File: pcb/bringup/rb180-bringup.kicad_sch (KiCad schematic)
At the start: 55 parts, among them J1 GT-USB-7010B, J2 Conn_02x03, J3 Conn_02x01, SW1 SKRPACE010, SW2 SKRPACE010, U2 NCP115ASN330, U4 W25Q128JVSS, U6 SN74LVC8T245, U7 SN74LVC8T245, U8 SN74LVC8T245, Y1 12 MHz

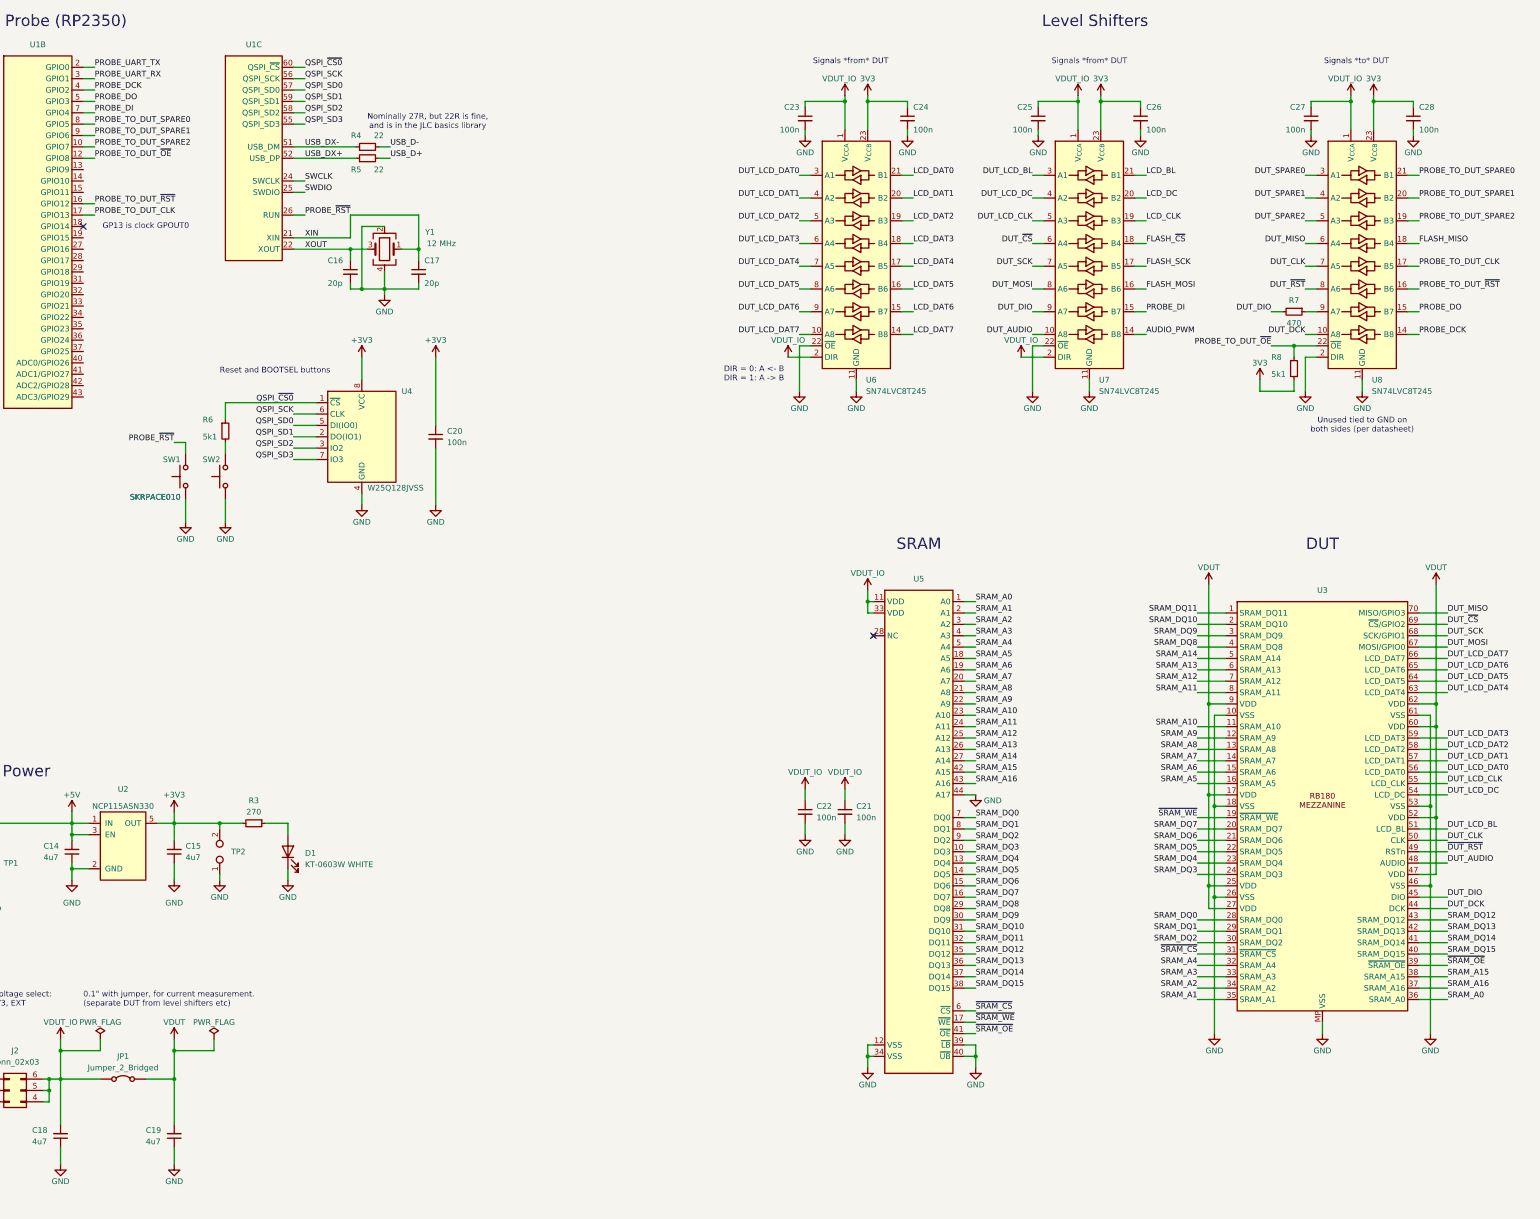
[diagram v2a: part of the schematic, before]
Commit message: Add LCD header and control muxing jumpers
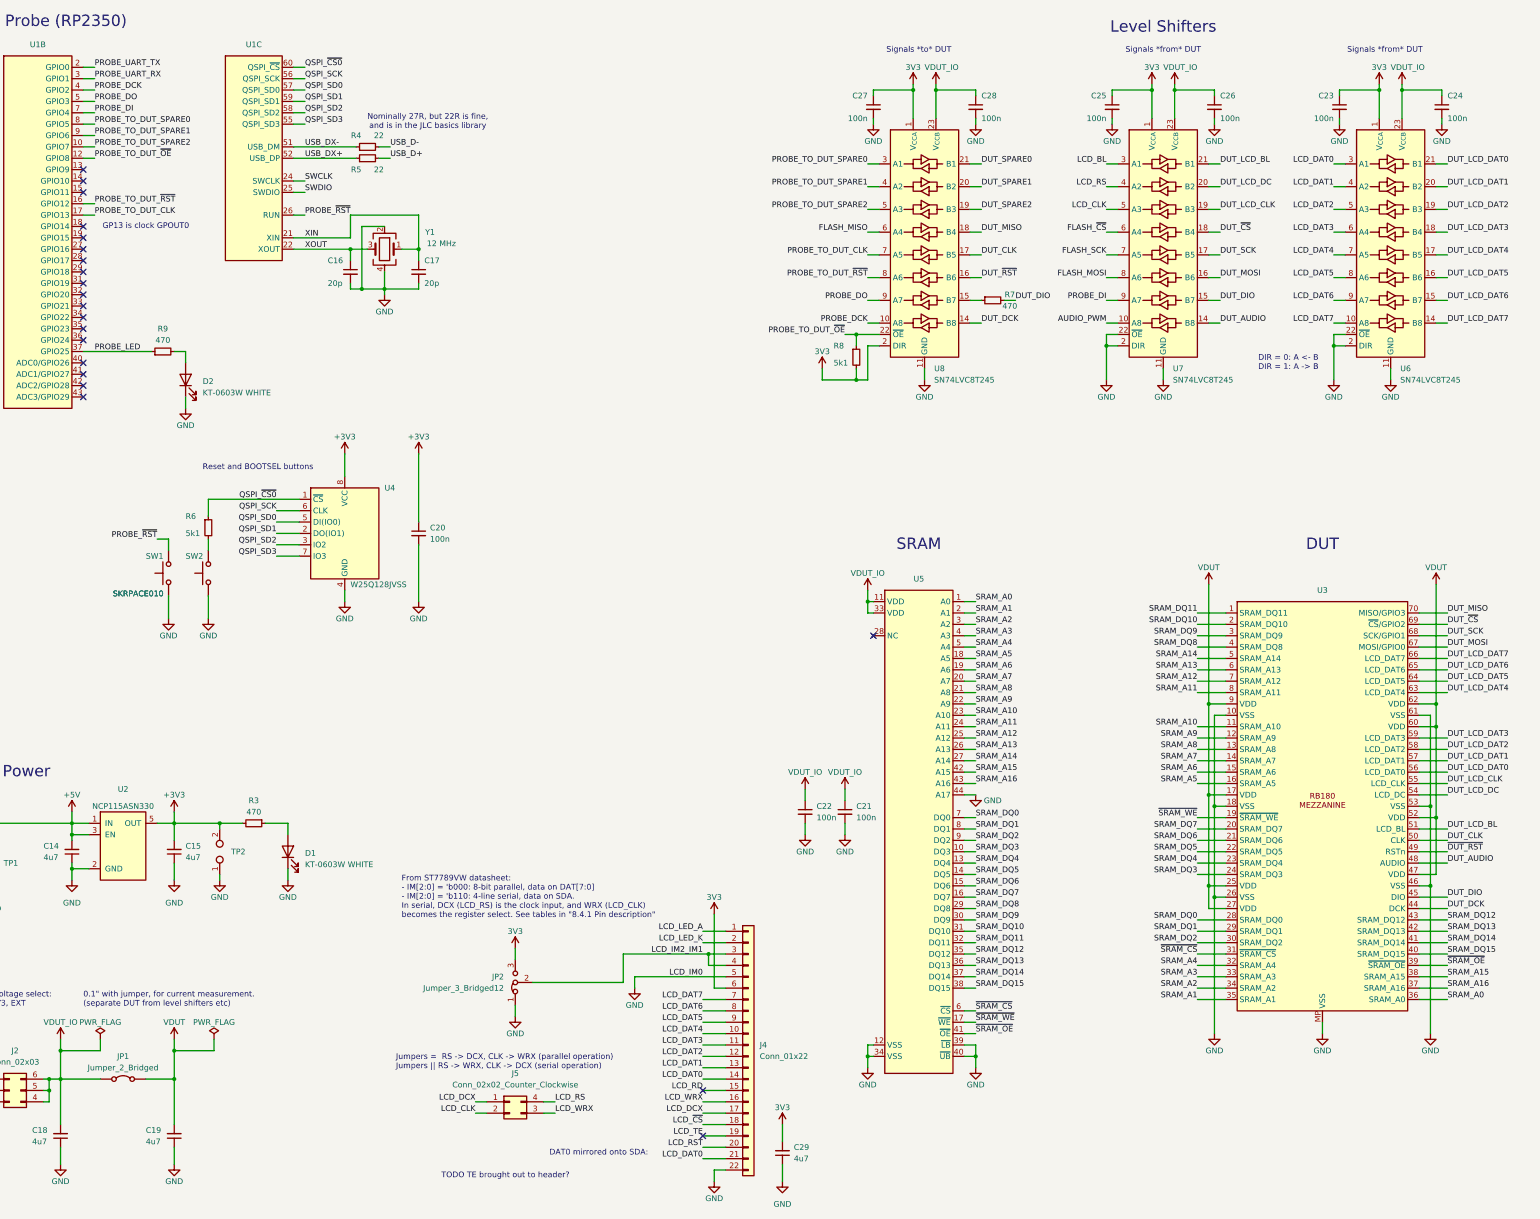
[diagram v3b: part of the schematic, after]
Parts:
- added C29: 4u7, Capacitor_SMD:C_0402_1005Metric, symbol Device:C_Small
- added D2: KT-0603W WHITE, LED_SMD:LED_0603_1608Metric, symbol Device:LED
- added J4: Conn_01x22, symbol Connector_Generic:Conn_01x22
- added J5: Conn_02x02_Counter_Clockwise, symbol Connector_Generic:Conn_02x02_Counter_Clockwise
- added JP2: Jumper_3_Bridged12, symbol Jumper:Jumper_3_Bridged12
- added R9: 470, Resistor_SMD:R_0402_1005Metric, symbol Device:R_Small
- R3: value 270 -> 470; LCSC C352448 -> (none)
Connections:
- net LCD_DC is gone; now on net DUT_LCD_DC: U7.20 (B2)
- net 3V3: now also C23.1, C25.1, C27.1, U6.1 (V_{CCA}), U7.1 (V_{CCA}), U8.1 (V_{CCA}), U8.2 (DIR), C29.2, J4.6 (Pin_6), JP2.3 (B); no longer C24.1, C26.1, C28.1, U6.23 (V_{CCB}), U6.24 (V_{CCB}), U7.23 (V_{CCB}), U7.24 (V_{CCB}), U8.23 (V_{CCB}), U8.24 (V_{CCB})
- net AUDIO_PWM: now also U7.10 (A8); no longer U7.14 (B8)
- net DUT_AUDIO: now also U7.14 (B8); no longer U7.10 (A8)
- net DUT_CLK: now also U8.17 (B5); no longer U8.7 (A5)
- net DUT_DCK: now also U8.14 (B8); no longer U8.10 (A8)
- net DUT_DIO: now also U7.15 (B7); no longer U7.9 (A7)
- net DUT_LCD_BL: now also U7.21 (B1); no longer U7.3 (A1)
- net DUT_LCD_CLK: now also U7.19 (B3); no longer U7.5 (A3)
- net DUT_LCD_DAT0: now also U6.21 (B1); no longer U6.3 (A1)
- net DUT_LCD_DAT1: now also U6.20 (B2); no longer U6.4 (A2)
- net DUT_LCD_DAT2: now also U6.19 (B3); no longer U6.5 (A3)
- net DUT_LCD_DAT3: now also U6.18 (B4); no longer U6.6 (A4)
- net DUT_LCD_DAT4: now also U6.17 (B5); no longer U6.7 (A5)
- net DUT_LCD_DAT5: now also U6.16 (B6); no longer U6.8 (A6)
- net DUT_LCD_DAT6: now also U6.15 (B7); no longer U6.9 (A7)
- net DUT_LCD_DAT7: now also U6.14 (B8); no longer U6.10 (A8)
- net DUT_LCD_DC: no longer U7.4 (A2)
- net DUT_MISO: now also U8.18 (B4); no longer U8.6 (A4)
- net DUT_MOSI: now also U7.16 (B6); no longer U7.8 (A6)
- net DUT_SCK: now also U7.17 (B5); no longer U7.7 (A5)
- net DUT_SPARE0: now also U8.21 (B1); no longer U8.3 (A1)
- net DUT_SPARE1: now also U8.20 (B2); no longer U8.4 (A2)
- net DUT_SPARE2: now also U8.19 (B3); no longer U8.5 (A3)
- net DUT_~{CS}: now also U7.18 (B4); no longer U7.6 (A4)
- net DUT_~{RST}: now also U8.16 (B6); no longer U8.8 (A6)
- net FLASH_MISO: now also U8.6 (A4); no longer U8.18 (B4)
- net FLASH_MOSI: now also U7.8 (A6); no longer U7.16 (B6)
- net FLASH_SCK: now also U7.7 (A5); no longer U7.17 (B5)
- net FLASH_~{CS}: now also U7.6 (A4); no longer U7.18 (B4)
- net GND: now also U6.2 (DIR), U7.2 (DIR), C29.1, D2.1 (K), J4.22 (Pin_22), J4.5 (Pin_5), JP2.1 (A); no longer U8.2 (DIR)
- net LCD_BL: now also U7.3 (A1); no longer U7.21 (B1)
- net LCD_CLK: now also U7.5 (A3), J5.2 (Pin_2); no longer U7.19 (B3)
- net LCD_DAT0: now also U6.3 (A1), J4.14 (Pin_14), J4.21 (Pin_21); no longer U6.21 (B1)
- net LCD_DAT1: now also U6.4 (A2), J4.13 (Pin_13); no longer U6.20 (B2)
- net LCD_DAT2: now also U6.5 (A3), J4.12 (Pin_12); no longer U6.19 (B3)
- net LCD_DAT3: now also U6.6 (A4), J4.11 (Pin_11); no longer U6.18 (B4)
- net LCD_DAT4: now also U6.7 (A5), J4.10 (Pin_10); no longer U6.17 (B5)
- net LCD_DAT5: now also U6.8 (A6), J4.9 (Pin_9); no longer U6.16 (B6)
- net LCD_DAT6: now also U6.9 (A7), J4.8 (Pin_8); no longer U6.15 (B7)
- net LCD_DAT7: now also U6.10 (A8), J4.7 (Pin_7); no longer U6.14 (B8)
- net PROBE_DCK: now also U8.10 (A8); no longer U8.14 (B8)
- net PROBE_DI: now also U7.9 (A7); no longer U7.15 (B7)
- net PROBE_DO: now also U8.9 (A7); no longer U8.15 (B7)
- net PROBE_TO_DUT_CLK: now also U8.7 (A5); no longer U8.17 (B5)
- net PROBE_TO_DUT_SPARE0: now also U8.3 (A1); no longer U8.21 (B1)
- net PROBE_TO_DUT_SPARE1: now also U8.4 (A2); no longer U8.20 (B2)
- net PROBE_TO_DUT_SPARE2: now also U8.5 (A3); no longer U8.19 (B3)
- net PROBE_TO_DUT_~{RST}: now also U8.8 (A6); no longer U8.16 (B6)
- net VDUT_IO: now also C24.1, C26.1, C28.1, U6.23 (V_{CCB}), U6.24 (V_{CCB}), U7.23 (V_{CCB}), U7.24 (V_{CCB}), U8.23 (V_{CCB}), U8.24 (V_{CCB}); no longer C23.1, C25.1, C27.1, U6.1 (V_{CCA}), U6.2 (DIR), U7.1 (V_{CCA}), U7.2 (DIR), U8.1 (V_{CCA})
- net at R7.1: now also U8.15 (B7); no longer U8.9 (A7)
- net PROBE_LED: now reaches U1.37 (GPIO25)
- net PROBE_LED: now also R9.1
- new net: D2.2 (A), R9.2
- new net LCD_DCX: J4.17 (Pin_17), J5.1 (Pin_1)
- new net LCD_IM2_IM1: J4.3 (Pin_3), J4.4 (Pin_4), JP2.2 (C)
- new net LCD_LED_A: J4.1 (Pin_1)
- new net LCD_LED_K: J4.2 (Pin_2)
- new net LCD_RD: J4.15 (Pin_15)
- new net LCD_RS: J5.4 (Pin_4), U7.4 (A2)
- new net LCD_RST: J4.20 (Pin_20)
- new net LCD_TE: J4.19 (Pin_19)
- new net LCD_WRX: J4.16 (Pin_16), J5.3 (Pin_3)
- new net LCD_~{CS}: J4.18 (Pin_18)
- no-connect marks 4 -> 23
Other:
- note added: "DAT0 mirrored onto SDA:"
- note added: "From ST7789VW datasheet: - IM[2:0] = 'b000: 8-bit parallel, data on DAT[7:0] - IM[2:0] = 'b110: 4-line serial, data on SDA. In serial, DCX (LCD_RS) is the clock input, and WRX (LCD_CLK) becomes the register select. See tables in "8.4.1 Pin description""
- note added: "Jumpers = RS -> DCX, CLK -> WRX (parallel operation) Jumpers || RS -> WRX, CLK -> DCX (serial operation)"
- note added: "TODO TE brought out to header?"
- note removed: "Unused tied to GND on both sides (per datasheet)"
- moved on the sheet: C20, C23, C24, C25, C26, C27, C28, R6, R7, R8, SW1, SW2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

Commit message: Mostly feature-complete
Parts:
- removed C12, C13: 100n, Capacitor_SMD:C_0402_1005Metric, symbol Device:C_Small
- added C30: 470n, Capacitor_SMD:C_0402_1005Metric, symbol Device:C_Small
- added J6, J7: Conn_02x09_Odd_Even, symbol Connector_Generic:Conn_02x09_Odd_Even
- added J8: (no value), symbol Connector_Generic:Conn_02x03_Odd_Even
- added R10: 5k1, Resistor_SMD:R_0402_1005Metric, symbol Device:R_Small
- added R11: 22, Resistor_SMD:R_0402_1005Metric, symbol Device:R_Small
- added TP3: (no value), ammo-board:TP_1x02_P1.00mm, symbol Connector:TestPoint_2Pole
- added U9: W25Q128JVSS, Package_SO:SOIC-8_3.9x4.9mm_P1.27mm, symbol Memory_Flash:W25Q32JVSS
- C1, C2, C20, C21, C22, C23, C24, C25, C26, C27, C28, C3, C4, C5, C6, C7, C8, C9: value 100n -> 470n; LCSC C1525 -> C47339
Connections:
- net +3V3 is gone; now on net 3V3: C15.2, C2.1, C20.1, C4.1, C6.1, C7.1, C8.1, C9.1, J2.2 (Pin_2), R3.2, TP2.2, U1.1 (IOVDD), U1.11 (IOVDD), U1.20 (IOVDD), U1.30 (IOVDD), U1.38 (IOVDD), U1.44 (ADC_IOVDD), U1.45 (IOVDD), U1.46 (VREG_AVDD), U1.53 (USB_OTP_VDD), U1.54 (QSPI_IOVDD), U2.5 (OUT), U4.8 (VCC)
- net LCD_LED_K is gone; now on net GND: J4.2 (Pin_2)
- net LCD_RD is gone; now on net 3V3: J4.15 (Pin_15)
- net LCD_RST is gone; now on net PROBE_TO_DUT_~{RST}: J4.20 (Pin_20)
- net +1V1: now also TP3.2
- net 3V3: now also C30.1, J7.1 (Pin_1), J8.6 (Pin_6), U9.3 (IO2), U9.7 (IO3), U9.8 (VCC)
- net AUDIO_PWM: now also J7.15 (Pin_15)
- net FLASH_MISO: now also J8.4 (Pin_4), U9.2 (DO(IO1))
- net FLASH_MOSI: now also J8.2 (Pin_2), U9.5 (DI(IO0))
- net FLASH_SCK: now also J8.3 (Pin_3), U9.6 (CLK)
- net FLASH_~{CS}: now also J8.1 (Pin_1), U9.1 (~{CS})
- net GND: now also C30.2, J6.1 (Pin_1), J6.17 (Pin_17), J6.18 (Pin_18), J6.2 (Pin_2), J7.17 (Pin_17), J7.18 (Pin_18), J7.2 (Pin_2), J8.5 (Pin_5), R10.2, TP3.1, U9.4 (GND)
- net LCD_BL: now also J7.16 (Pin_16), R11.1
- net LCD_CLK: now also J7.14 (Pin_14)
- net LCD_DAT0: now also J7.9 (Pin_9)
- net LCD_DAT1: now also J7.10 (Pin_10)
- net LCD_DAT2: now also J7.7 (Pin_7)
- net LCD_DAT3: now also J7.8 (Pin_8)
- net LCD_DAT4: now also J7.5 (Pin_5)
- net LCD_DAT5: now also J7.6 (Pin_6)
- net LCD_DAT6: now also J7.3 (Pin_3)
- net LCD_DAT7: now also J7.4 (Pin_4)
- net LCD_LED_A: now also R11.2
- net LCD_RS: now also J7.12 (Pin_12)
- net LCD_TE: now also J7.13 (Pin_13)
- net LCD_~{CS}: now also J7.11 (Pin_11), R10.1
- net PROBE_DCK: now also J6.5 (Pin_5)
- net PROBE_DI: now also J6.7 (Pin_7)
- net PROBE_DO: now also J6.6 (Pin_6)
- net PROBE_TO_DUT_CLK: now also J6.10 (Pin_10)
- net PROBE_TO_DUT_~{OE}: now also J6.8 (Pin_8)
- net PROBE_TO_DUT_~{RST}: now also J6.9 (Pin_9)
- net PROBE_UART_RX: now also J6.4 (Pin_4)
- net PROBE_UART_TX: now also J6.3 (Pin_3)
- net SWCLK: now also J6.15 (Pin_15)
- net SWDIO: now also J6.16 (Pin_16)
- net PROBE_SPARE0: now reaches U1.27 (GPIO16)
- net PROBE_SPARE0: now also J6.11 (Pin_11)
- net PROBE_SPARE1: now reaches U1.28 (GPIO17)
- net PROBE_SPARE1: now also J6.12 (Pin_12)
- net PROBE_SPARE2: now reaches U1.29 (GPIO18)
- net PROBE_SPARE2: now also J6.13 (Pin_13)
- net PROBE_SPARE3: now reaches U1.31 (GPIO19)
- net PROBE_SPARE3: now also J6.14 (Pin_14)
- no-connect marks 23 -> 18
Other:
- note added: "AUDIO_PWM is brought out as a potentially spare output that we could patch into ~{CS} (holding constant low is cheeky)"
- note added: "DUT Flash"
- note added: "Nominally 27R, but 22R is in the JLC basics library"
- note added: "Probe Flash"
- note removed: "Nominally 27R, but 22R is fine, and is in the JLC basics library"
- note removed: "TODO TE brought out to header?"
- company: (none) -> Luke Wren
- title: (none) -> RB180 Bringup Board
- moved on the sheet: C14, C15, C20, C21, C22, D1, J5, JP2, R3, R6, SW1, SW2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

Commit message: Add audio output and push buttons
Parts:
- added C31: 68n, Capacitor_SMD:C_0402_1005Metric, symbol Device:C_Small
- added C32, C33: 4u7, Capacitor_SMD:C_0402_1005Metric, symbol Device:C_Small
- added J9: SHOU HAN PJ-320D, ammo-board:TRRS-PJ-320D, symbol Connector_Audio:AudioJack4
- added R12: 470, Resistor_SMD:R_0402_1005Metric, symbol Device:R_Small
- added R13, R15, R16, R17, R18, R19, R20, R21, R22: 5k1, Resistor_SMD:R_0402_1005Metric, symbol Device:R_Small
- added R14: 220, esistor_SMD:R_0402_1005Metric, symbol Device:R_Small
- added SW10, SW3, SW4, SW5, SW6, SW7, SW8, SW9: SKRPACE010, ammo-board:SW_SPST_PTS815, symbol Switch:SW_Push
- D1, D2: value KT-0603W WHITE -> KT-0603W
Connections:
- net AUDIO_PWM: now also R12.2
- net DUT_LCD_DAT0: now also R22.1
- net DUT_LCD_DAT1: now also R21.1
- net DUT_LCD_DAT2: now also R20.1
- net DUT_LCD_DAT3: now also R19.1
- net DUT_LCD_DAT4: now also R18.1
- net DUT_LCD_DAT5: now also R17.1
- net DUT_LCD_DAT6: now also R16.1
- net DUT_LCD_DAT7: now also R13.1
- net GND: now also C31.2, J9.S, R14.1, R15.1, SW10.2, SW3.2, SW4.2, SW5.2, SW6.2, SW7.2, SW8.2, SW9.2
- new net: R16.2, SW4.1
- new net: C31.1, C32.1, C33.1, R12.1, R14.2
- new net: R19.2, SW7.1
- new net: C32.2, C33.2, J9.T, R15.2
- new net: R13.2, SW3.1
- new net: R22.2, SW10.1
- new net: R17.2, SW5.1
- new net: R21.2, SW9.1
- new net: R20.2, SW8.1
- new net: R18.2, SW6.1
- no-connect marks 18 -> 20
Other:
- note added: "DUT Peripherals"
- note added: "Debug Headers"
- note added: "From DUT"
- note added: "High cutoff: 15.6 kHz Low cutoff (Rload = 32): 93 Hz"
- note added: "Jumpers = RS -> DCX, CLK -> WRX (parallel) Jumpers || RS -> WRX, CLK -> DCX (serial)"
- note added: "To DUT"
- note added: "Upstream of level shifters: sample during VBLANK by tristating (pad pullup 90k ~ 200k)"
- note removed: "Jumpers = RS -> DCX, CLK -> WRX (parallel operation) Jumpers || RS -> WRX, CLK -> DCX (serial operation)"
- note removed: "Probe Flash"
- note removed: "Signals *from* DUT"
- note removed: "Signals *to* DUT"
- moved on the sheet: C10, C11, C14, C15, C16, C17, C18, C19, C20, C21, C22, C23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

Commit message: Fix some ERCs
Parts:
- added J10: Conn_02x02_Counter_Clockwise, symbol Connector_Generic:Conn_02x02_Counter_Clockwise
- U3: renamed from U4; footprint Package_SO:SOIC-8_3.9x4.9mm_P1.27mm -> Package_SO:SOIC-8_5.3x5.3mm_P1.27mm
- U4: renamed from U9; footprint Package_SO:SOIC-8_3.9x4.9mm_P1.27mm -> Package_SO:SOIC-8_5.3x5.3mm_P1.27mm
- renumbered C14 to C12, C18 to C13, C15 to C14, C19 to C15, C20 to C18, C31 to C19, C33 to C20, C32 to C21, C29 to C22, C30 to C23, C27 to C24, C21 to C25, C22 to C26, C28 to C27, C25 to C28, C26 to C29, C23 to C30, C24 to C31, D2 to D1, D1 to D2, J3 to J2, J2 to J3, J5 to J4, J9 to J5, J4 to J9, R15 to R10, R10 to R11, R11 to R12, R16 to R14, R17 to R15, R18 to R16, R19 to R17, R20 to R18, R21 to R19, R22 to R20, R8 to R21, R7 to R22, R9 to R3, R6 to R4, R3 to R5, R4 to R6, R5 to R7, R12 to R8, R14 to R9, TP3 to TP1, TP1 to TP2, TP2 to TP3, U8 to U5, U5 to U6, U3 to U8, U6 to U9
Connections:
- net ~{DUT_RST} is gone; now on net DUT_~{RST}: U8.49 (RSTn)
- net DUT_SPARE0: now also J10.1 (Pin_1)
- net DUT_SPARE1: now also J10.4 (Pin_4)
- net DUT_SPARE2: now also J10.2 (Pin_2)
- net GND: now also J10.3 (Pin_3)
- no-connect marks 20 -> 19
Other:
- note added: "LCD_IM0"
- note added: "LCD_LED_K"
- note added: "LCD_RDX"
- moved on the sheet: U3, U4
